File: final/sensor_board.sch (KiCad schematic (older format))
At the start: 71 parts, among them J2 USB_microB_2040002-1, J3 Arduino_ICSP, J4 Conn_01x02_Male, J5 Conn_01x15_Male, J6 Conn_01x15_Male, J7 BT CONFIG, SW1 SW_DIP_x01, U10 BQ24075, U11 BQ27441-G1, U2 TXS0104E, U3 MCP1702T-3302E/CBCT-ND, U4 FT232RL, U5 RN4871, U6 MCP1702T-5002E_CB, U7 TPS2113ADRBR, U8 US5881, U9 ATMEGA328PB-ANR, Y1 16MHz

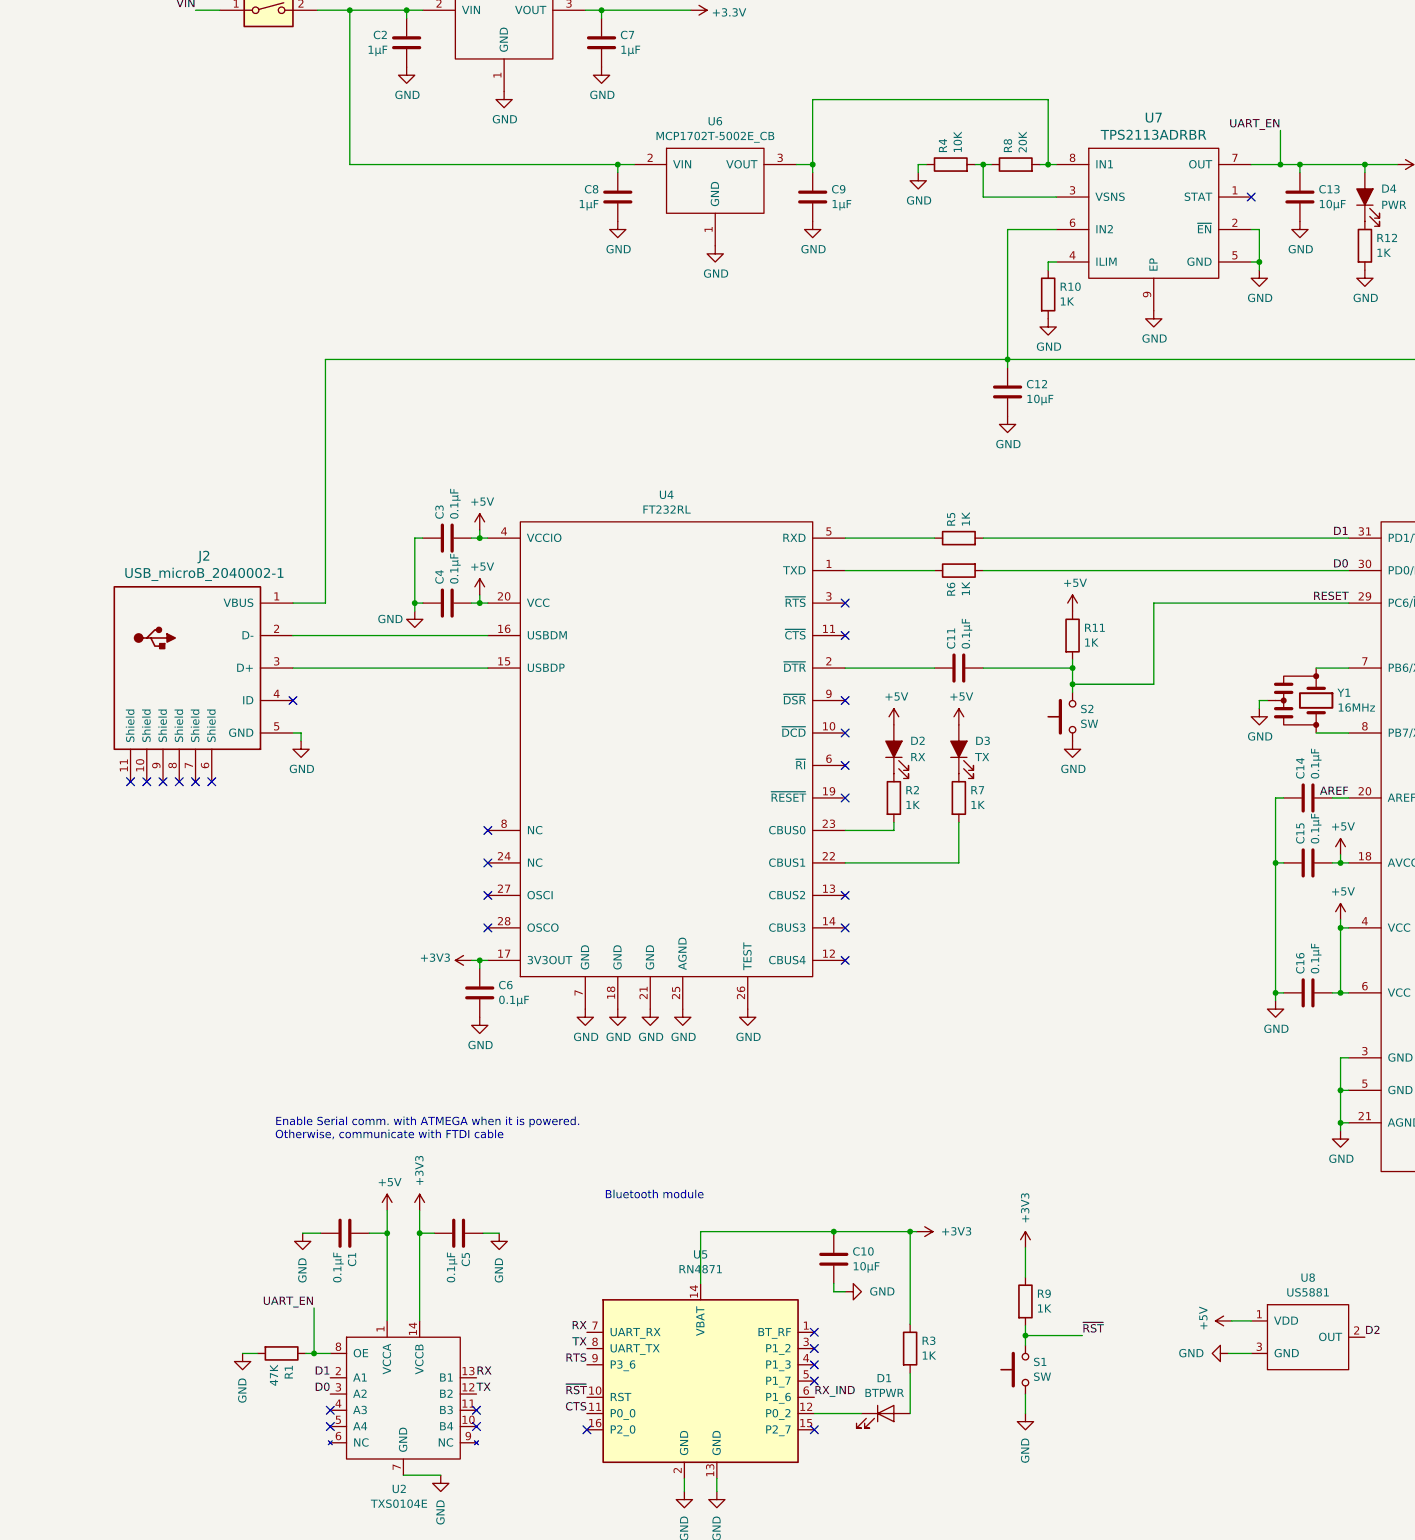
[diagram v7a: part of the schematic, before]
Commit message: Add inverter and change enable
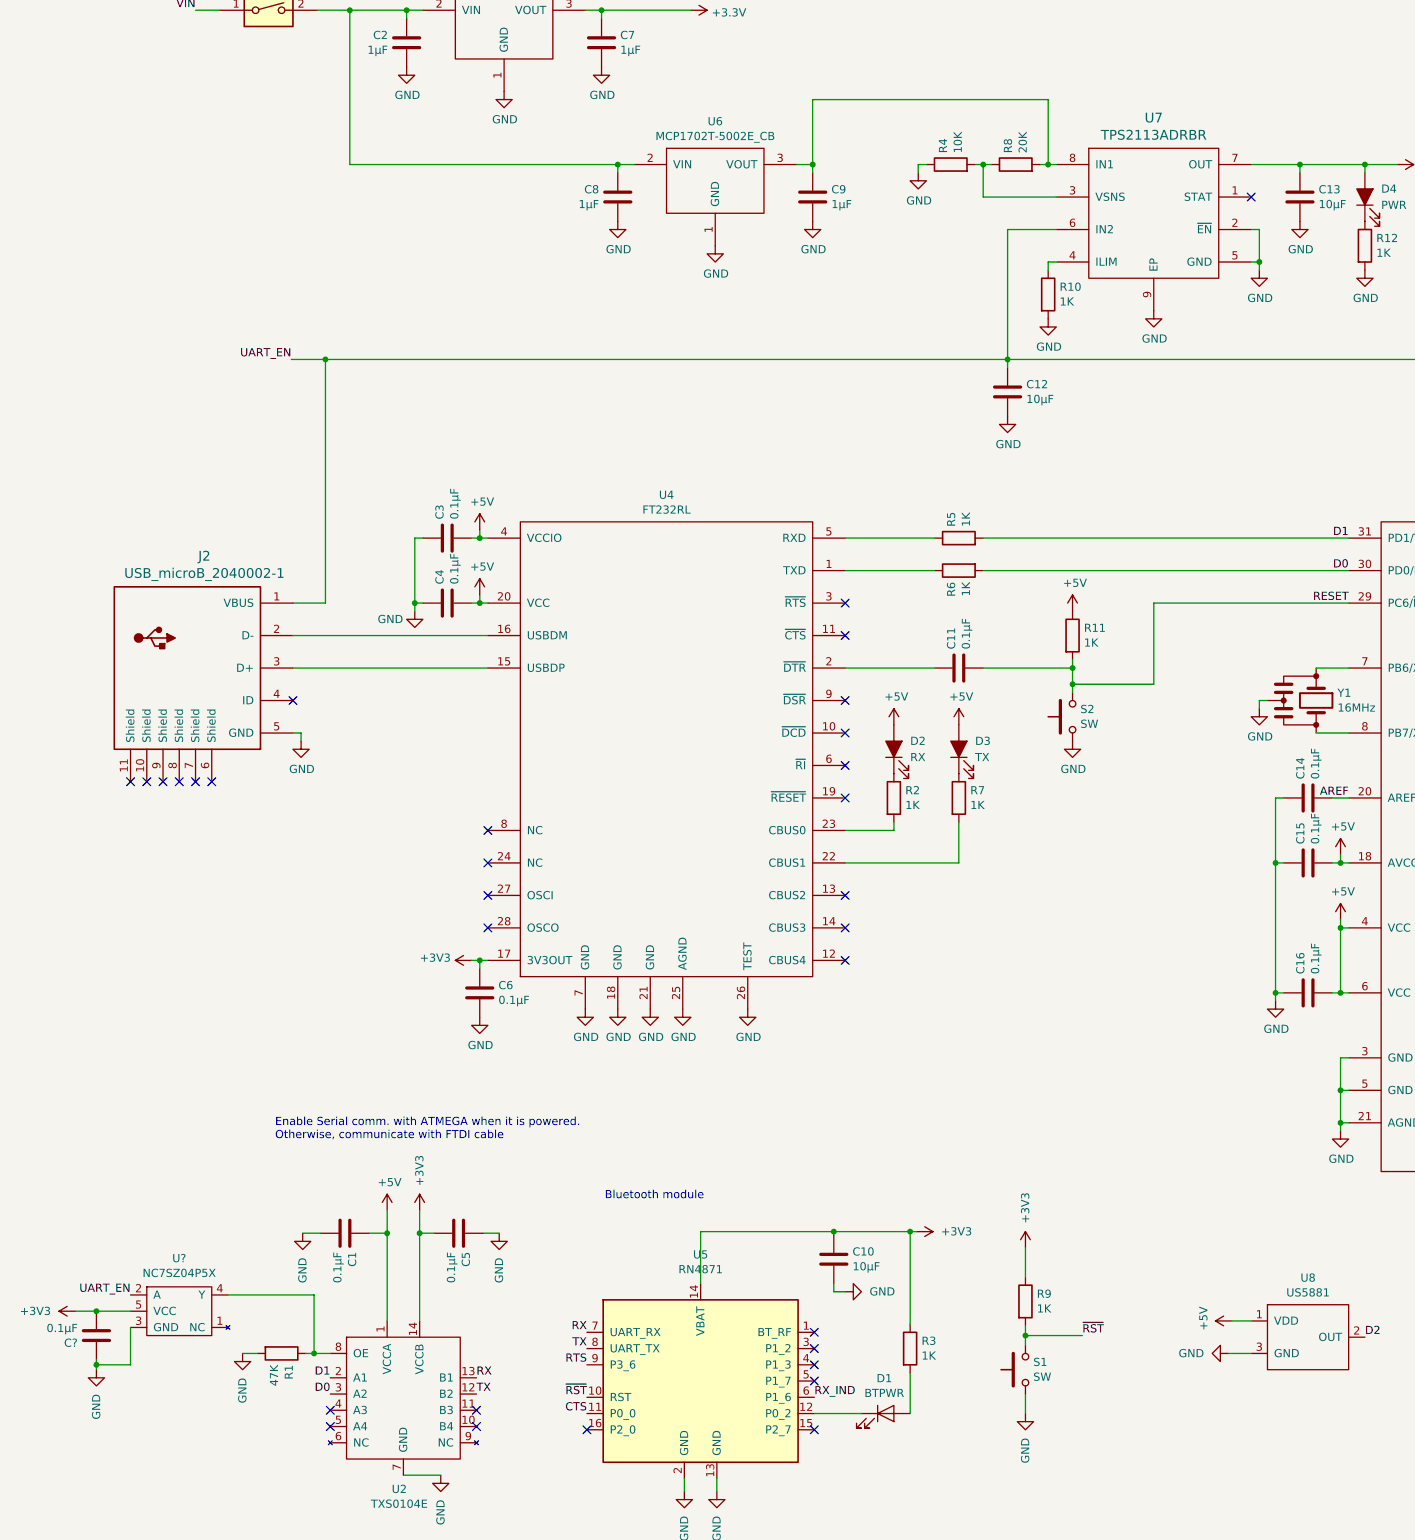
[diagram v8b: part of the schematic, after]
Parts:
- added C?: 0.1µF, Capacitor_SMD:C_0603_1608Metric, symbol Device:C
- added U?: NC7SZ04P5X, symbol final:NC7SZ04P5X
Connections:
- net +3V3: now also C?.2, U?.5 (VCC)
- net +5V: no longer R1.1, U2.8 (OE)
- net GND: now also C?.1, U?.3 (GND)
- net UART_EN: now reaches C12.1, C17.2, J2.1 (VBUS), U10.13 (IN), U7.6 (IN2)
- net UART_EN: now also U?.2 (A)
- new net: R1.1, U2.8 (OE), U?.4 (Y)
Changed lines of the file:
@@
 $EndComp
-Wire Wire Line
-	8250 2000 8430 2000
 Wire Wire Line
 	8950 2050 8950 2000
@@
 Wire Wire Line
 	2430 9320 2480 9320
-Text Label 8430 1790 2    50   ~ 0
+Text Label 2340 3200 2    50   ~ 0
 UART_EN
-Text Label 2480 9040 2    50   ~ 0
+Text Label 1350 8960 2    50   ~ 0
 UART_EN
-Wire Wire Line
-	2480 9040 2480 9320
 Connection ~ 2480 9320
 Wire Wire Line
@@
 Text Notes 2240 8010 0    50   ~ 0
 Enable Serial comm. with ATMEGA when it is powered.\nOtherwise, communicate with FTDI cable
-Wire Wire Line
-	8430 1790 8430 2000
-Connection ~ 8430 2000
-Wire Wire Line
-	8430 2000 8550 2000
 Text Notes 4270 8380 0    50   ~ 0
 Bluetooth module
@@
 Text Notes 14800 4250 0    50   ~ 0
 Battery Header
+$Comp
+L final:NC7SZ04P5X U?
+U 1 1 5CB62293
+P 1650 9060
+F 0 "U?" H 1650 9385 50  0000 C CNN
+F 1 "NC7SZ04P5X" H 1650 9294 50  0000 C CNN
+F 2 "" H 1650 9060 50  0001 C CNN
+F 3 "" H 1650 9060 50  0001 C CNN
+	1    1650 9060
+	1    0    0    -1
+$EndComp
+Wire Wire Line
+	1950 8960 2480 8960
+Wire Wire Line
+	2480 8960 2480 9320
+$Comp
+L power:+3V3 #PWR?
+U 1 1 5CB88CF2
+P 1010 9060
+F 0 "#PWR?" H 1010 8910 50  0001 C CNN
+F 1 "+3V3" V 1010 9210 50  0000 L CNN
+F 2 "" H 1010 9060 50  0001 C CNN
+F 3 "" H 1010 9060 50  0001 C CNN
+	1    1010 9060
+	0    -1   1    0
+$EndComp
+$Comp
+L power:GND #PWR?
+U 1 1 5CB88E65
+P 1140 9420
+F 0 "#PWR?" H 1140 9170 50  0001 C CNN
+F 1 "GND" V 1140 9270 50  0000 R CNN
+F 2 "" H 1140 9420 50  0001 C CNN
+F 3 "" H 1140 9420 50  0001 C CNN
+	1    1140 9420
+	1    0    0    -1
+$EndComp
+Wire Wire Line
+	8250 2000 8550 2000
+Wire Wire Line
+	2340 3200 2550 3200
+Connection ~ 2550 3200
+Wire Wire Line
+	1350 9060 1140 9060
+$Comp
+L Device:C C?
+U 1 1 5CBD6DA1
+P 1140 9210
+F 0 "C?" H 1255 9256 50  0000 L CNN
+F 1 "0.1µF" H 1255 9165 50  0000 L CNN
+F 2 "Capacitor_SMD:C_0603_1608Metric" H 1178 9060 50  0001 C CNN
+F 3 "~" H 1140 9210 50  0001 C CNN
+	1    1140 9210
+	-1   0    0    1
+$EndComp
+Connection ~ 1140 9060
+Wire Wire Line
+	1140 9060 1010 9060
+Wire Wire Line
+	1140 9420 1140 9390
+Wire Wire Line
+	1350 9160 1350 9390
+Wire Wire Line
+	1350 9390 1140 9390
+Connection ~ 1140 9390
+Wire Wire Line
+	1140 9390 1140 9360
 $EndSCHEMATC
